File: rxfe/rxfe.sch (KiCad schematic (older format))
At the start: 84 parts, among them J1 SMA, J2 SMA, J3 4610X-AP1-103LF, P1 CONN_8X2, P2 CONN_2, U1 SKY12347, U10 SMP1330-005LF, U11 SMP1330-005LF, U12 SMP1330-005LF, U13 7805, U14 TCM809, U2 74HC04, U3 SCLF-25, U4 HMC595, U5 HMC595, U6 MGA-61563, U7 MGA-61563, U8 HMC595, U9 HMC595

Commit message: cleanups on rxfe
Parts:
- C1, C10, C11, C12, C13, C14, C15, C16, C17, C18, C19, C2, C20, C21, C22, C23, C24, C25, C26, C27, C28, C3, C4, C5, C9, D1, L4, L5, L6, L7, R1, R10, R11, R12, R13, R14, R2, R3, R4, R5, R7, R8, R9: footprint SMD_Packages:SM0805 -> SMD_Packages:SMD-0805
- C31, C32, C33, C34, C35: renamed from C?; footprint SMD_Packages:SM0805 -> SMD_Packages:SMD-0805
- C6, C7, C8, L1, L2, L3: footprint SMD_Packages:SM1210 -> SMD_Packages:SMD-1210
- H1, H2, H3, H4: renamed from H?; footprint (none) -> Mounting_Holes:MountingHole_6-5mm
- J1, J2: footprint sma:sma -> local:SMA_5-1814832-1
- L8: renamed from L?; footprint SMD_Packages:SM0805 -> SMD_Packages:SMD-0805
- P1: footprint Connect:VASCH10x2 -> Connect:VASCH8x2
- R15, R6: renamed from R?; footprint SMD_Packages:SM0805 -> SMD_Packages:SMD-0805
- U10, U11, U12: footprint SMD_Packages:SOT23 -> SMD_Packages:SOT-23
- U13: footprint (none) -> Housings_SOT-89:SOT89-3_Housing
- U14: footprint (none) -> SMD_Packages:SOT-23
- U15: renamed from U?; footprint SMD_Packages:SOT23 -> SMD_Packages:SOT-23
- U4, U5, U8, U9: footprint SMD_Packages:SOT23_6 -> SMD_Packages:SOT-23-6
- gave numbers to parts that had none: 1

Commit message: moved rf amps from control board to rxfe and driver
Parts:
- removed L8: 10 uH, SMD_Packages:SMD-0805, symbol INDUCTOR_SMALL
- removed P2: CONN_2, Connect:PINHEAD1-2, symbol CONN_2
- removed R13: 0, SMD_Packages:SMD-0805, symbol R
- removed R14: DNP, SMD_Packages:SMD-0805, symbol R
- removed R15: 1k, SMD_Packages:SMD-0805, symbol R
- removed U11, U15: SMP1330-005LF, SMD_Packages:SOT-23, symbol SMP1330-005LF
- removed U13: 7805, Housings_SOT-89:SOT89-3_Housing, symbol 7805
- removed U16, U6, U7: MGA-61563, Housings_SOT-23_SOT-143_TSOT-6:SC70-6, symbol MGA-61563
- added C36: 1 uF, SMD_Packages:SMD-0805, symbol C
- added J4: SMA, local:SMA_5-1814832-1, symbol SMA
- added K1: CONN_3, symbol CONN_3
- added U11: LTC1983-5, symbol LTC1983-5
- added U13: LDO_78XX, symbol LDO_78XX
- added U15, U16: GALI-84+, symbol HMC475
- added U6: MAR-8ASM+, symbol MAR-8ASM+
- added U7: SWMA-2-50DR+, symbol SWMA-2-50DR+
- C12, C14: value DNP -> 22 nF
- C15, C17, C21, C4: value 20 nF -> 22 nF
- C16, C18, C20, C22: value 100 pF -> 22 nF
- C19: value 20 nF -> 100 nF
- C31: value 22 nF -> 100 nF
- C32: value 100 pF -> 100 nF
- C33: value 20 nF -> 10 uF
- C34: value 100 pF -> 10 uF
- C35: value 22 nF -> 10 uF; footprint SMD_Packages:SMD-0805 -> SMD_Packages:SMD-1210
- C6: value 22 uF -> 10 uF
- L4, L5: value 0 -> 10 uH
- R10: value 0 -> 309
- R11: value DNP -> 309
- R12: value DNP -> 3.9; footprint SMD_Packages:SMD-0805 -> (none)
- R7: value 1k -> 0
- R9: value 1k -> 309
- U2: footprint SMD_Packages:TSSOP14 -> (none)
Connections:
- net labels added: -5V, T/R, VDD
- wire segments 247 -> 263
- no-connect marks 0 -> 2
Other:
- note added: "-5V switching regulator,\nfor high isolation T/R switch"
- note removed: "jumper to bypass first stage amp"
- moved on the sheet: C1, C10, C11, C13, C15, C17, C2, C23, C24, C25, C26, C29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

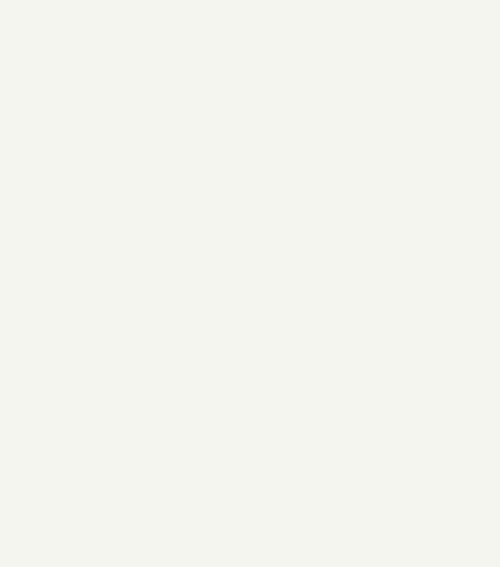
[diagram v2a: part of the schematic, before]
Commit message: DFM changes to boards - added fiducial markers and increase paste clearance
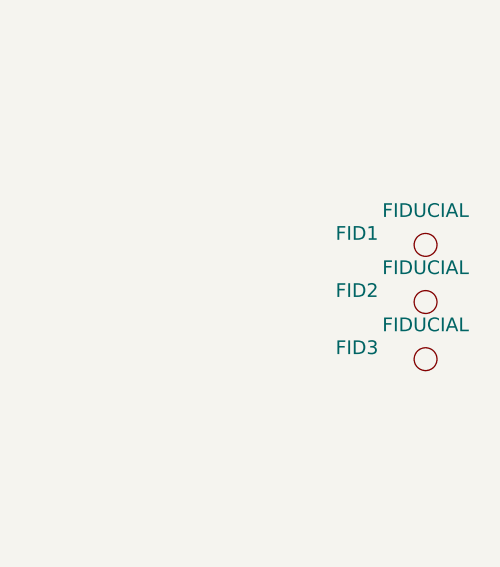
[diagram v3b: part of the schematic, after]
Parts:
- added FID1, FID2, FID3: FIDUCIAL, symbol MOUNTING_HOLE
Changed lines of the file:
@@
 	8450 15000 8450 14900
 Connection ~ 8450 14400
+$Comp
+L MOUNTING_HOLE FID1
+U 1 1 54D26C4B
+P 19650 3950
+F 0 "FID1" H 19350 4000 60  0000 C CNN
+F 1 "FIDUCIAL" H 19650 4100 60  0000 C CNN
+F 2 "" H 19650 3950 60  0000 C CNN
+F 3 "" H 19650 3950 60  0000 C CNN
+	1    19650 3950
+	1    0    0    -1
+$EndComp
+$Comp
+L MOUNTING_HOLE FID2
+U 1 1 54D26C67
+P 19650 4200
+F 0 "FID2" H 19350 4250 60  0000 C CNN
+F 1 "FIDUCIAL" H 19650 4350 60  0000 C CNN
+F 2 "" H 19650 4200 60  0000 C CNN
+F 3 "" H 19650 4200 60  0000 C CNN
+	1    19650 4200
+	1    0    0    -1
+$EndComp
+$Comp
+L MOUNTING_HOLE FID3
+U 1 1 54D26C72
+P 19650 4450
+F 0 "FID3" H 19350 4500 60  0000 C CNN
+F 1 "FIDUCIAL" H 19650 4600 60  0000 C CNN
+F 2 "" H 19650 4450 60  0000 C CNN
+F 3 "" H 19650 4450 60  0000 C CNN
+	1    19650 4450
+	1    0    0    -1
+$EndComp
 $EndSCHEMATC

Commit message: finished layout of DFM'ed driver ampifier board.. except still need to change connectors
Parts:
- C33, C34: footprint SMD_Packages:SMD-0805 -> SMD_Packages:SMD-1210_Pol
- C35: footprint SMD_Packages:SMD-1210 -> SMD_Packages:SMD-1210_Pol
- FID1, FID2, FID3: footprint (none) -> sdtransmitter:FID_1MM
- K1: footprint (none) -> localconn:3-647166-3
- L5, R10, R11, R9: footprint SMD_Packages:SMD-0805 -> SMD_Packages:SMD-1210
- R12: footprint (none) -> SMD_Packages:SMD-0805
- U11: footprint (none) -> SMD_Packages:SOT-23-6
- U13, U15, U16: footprint (none) -> Housings_SOT-89:SOT89-3_Housing
- U2: footprint (none) -> SMD_Packages:TSSOP14
- U6: footprint (none) -> sdtransmitter:WW107
- U7: footprint (none) -> sdtransmitter:DL1020

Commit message: DFM changes..
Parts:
- removed R7: 0, SMD_Packages:SMD-0805, symbol R
- added C37: 22 nF, SMD_Packages:SMD-0805, symbol C
- J1, J2, J4: footprint local:SMA_5-1814832-1 -> local:SMA_0732511350
- K1: footprint localconn:3-647166-3 -> sdtransmitter:0740991003
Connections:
- net at J4.1 (RF), R6.2: now also C37.2
- net at C14.2, R8.2: now also C37.1

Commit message: component footprint changes to simplify bom
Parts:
- removed C33: 10 uF, SMD_Packages:SMD-1210_Pol, symbol C
- removed R12: 3.9, SMD_Packages:SMD-0805, symbol R
- U4, U5, U9: value HMC595 -> MASWSS0179
- U8: value HMC595 -> MASWSS0179'
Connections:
- net -5V: now also C34.2, U11.2 (Vout)
- net GND: no longer U13.2 (GND)

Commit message: DFM changes after last protoype rev
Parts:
- removed C19, C2, C31, C32: 100 nF, SMD_Packages:SMD-0805, symbol C
- added R12, R7: 1k, SMD_Packages:SMD-0805, symbol R
- C1, C29, C5: value 100 nF -> 22 nF
- L4, L5, L6, L7: value 10 uH -> 3.9uH
- R10, R11: value 309 -> 93.1
- R9: value 309 -> 1k; footprint SMD_Packages:SMD-1210 -> SMD_Packages:SMD-0805
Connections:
- net GND: now also U13.2 (GND)
- net VDD: now also R12.1, R7.1
- net at L4.2, R9.2: now also R12.2, R7.2

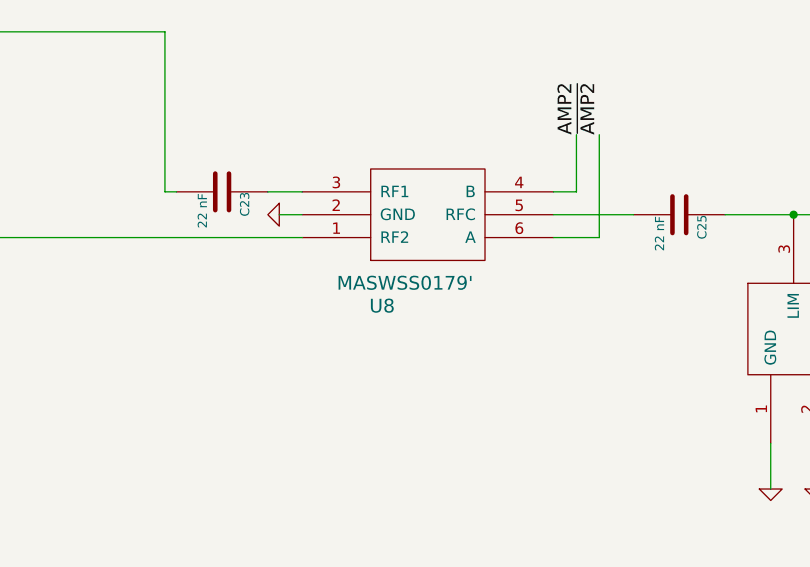
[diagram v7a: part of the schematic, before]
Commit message: updated schematic with distributor part numbers
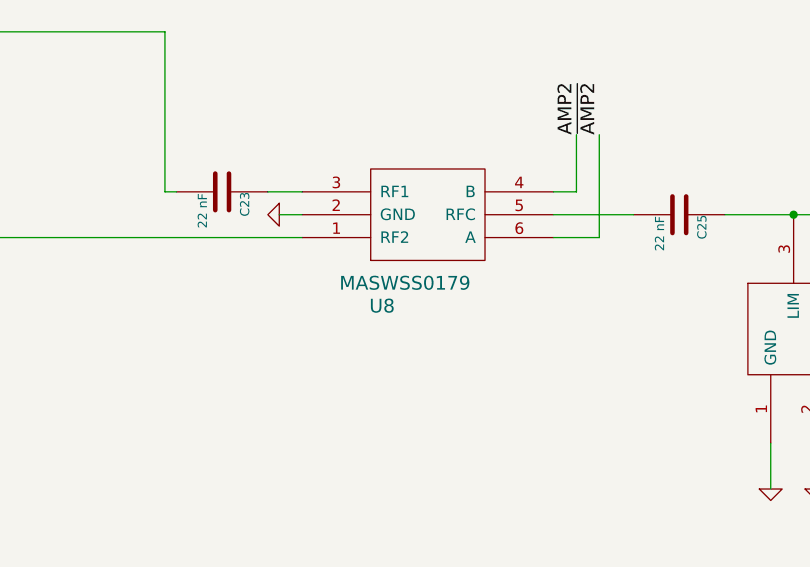
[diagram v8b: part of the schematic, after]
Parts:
- C1, C10, C11, C12, C13, C15, C16, C18, C20, C21, C22, C23, C24, C25, C26, C27, C28, C29, C3, C4, C5, C9: Dist Name (none) -> DigiKey; Dist PN (none) -> 490-1658-1-ND; MFG Name (none) -> MURATA ELECTRONICS (VA); MFG PN (none) -> GRM21BR72A223KA01L
- C14, C37: Dist PN (none) -> 490-1658-1-ND; MFG Name (none) -> MURATA ELECTRONICS (VA); MFG PN (none) -> GRM21BR72A223KA01L
- C17: Dist Name (none) -> DigiKey; MFG Name (none) -> MURATA ELECTRONICS (VA); MFG PN (none) -> GRM21BR72A223KA01L
- C30, C36: Dist Name (none) -> DigiKey; Dist PN (none) -> 445-8782-1-ND; MFG Name (none) -> TDK CORPORATION (VA); MFG PN (none) -> CGA4J3X7S2A105K125AE
- C34, C35: Dist Name (none) -> DigiKey; Dist PN (none) -> 478-3876-1-ND; MFG Name (none) -> AVX CORPORATION (VA); MFG PN (none) -> TAJB106M020RNJ
- C6: footprint SMD_Packages:SMD-1210 -> SMD_Packages:SMD-1210_Pol; Dist Name (none) -> DigiKey; Dist PN (none) -> 478-3876-1-ND; MFG Name (none) -> AVX CORPORATION (VA); MFG PN (none) -> TAJB106M020RNJ
- C7, C8: footprint SMD_Packages:SMD-1210 -> SMD_Packages:SMD-1206_Pol; Dist Name (none) -> DigiKey; Dist PN (none) -> 490-5278-1-ND; MFG Name (none) -> MURATA ELECTRONICS (VA); MFG PN (none) -> GRM31B5C2J681JW01L
- D1: Dist Name (none) -> DigiKey; Dist PN (none) -> 475-1278-1-ND; MFG Name (none) -> OSRAM OPTO SEMICONDUCTORS INC(VA); MFG PN (none) -> LS R976-NR-1
- J1, J2, J4: Dist Name (none) -> DigiKey; Dist PN (none) -> WM9357-ND; MFG Name (none) -> MOLEX INC; MFG PN (none) -> 732511350
- J3: Dist Name (none) -> DigiKey; Dist PN (none) -> 4610X-1-103LF-ND; MFG Name (none) -> BOURNS INC; MFG PN (none) -> 4610X-101-103LF
- K1: Dist Name (none) -> DigiKey; Dist PN (none) -> WM7203-ND; MFG Name (none) -> MOLEX INC; MFG PN (none) -> 740991003
- L1, L3: Dist Name (none) -> DigiKey; Dist PN (none) -> 445-16595-1-ND; MFG Name (none) -> TDK CORPORATION (VA); MFG PN (none) -> NLV32T-3R9J-EFD
- L2: Dist Name (none) -> DigiKey; Dist PN (none) -> PM1210-1R2J-RCCT-ND; MFG Name (none) -> BOURNS INC (VA); MFG PN (none) -> PM1210-1R2J-RC
- L4, L5, L6, L7: Dist Name (none) -> DigiKey
- P1: Dist Name (none) -> DigiKey; Dist PN (none) -> 3M11931-ND; MFG Name (none) -> 3M; MFG PN (none) -> 30316-6002HB
- R1, R12, R2, R3, R4, R5, R7: Dist Name (none) -> DigiKey; Dist PN (none) -> P1.00KCCT-ND; MFG Name (none) -> PANASONIC ELECTRONIC COMPONENTS (VA); MFG PN (none) -> ERJ-6ENF1001V
- R10, R11: Dist Name (none) -> DigiKey; Dist PN (none) -> P93.1FDKR-ND; MFG Name (none) -> PANASONIC ELECTRONIC COMPONENTS (VA); MFG PN (none) -> ERJ-8ENF93R1V
- R9: footprint SMD_Packages:SMD-0805 -> SMD_Packages:SMD-1210; Dist Name (none) -> DigiKey; Dist PN (none) -> P1.00KCCT-ND; MFG Name (none) -> PANASONIC ELECTRONIC COMPONENTS (VA); MFG PN (none) -> ERJ-6ENF1001V
- U1: Dist Name (none) -> DigiKey; Dist PN (none) -> 863-1298-1-ND; MFG Name (none) -> SKYWORKS SOLUTIONS INC (VA); MFG PN (none) -> SKY12347-362LF
- U10, U12: Dist Name (none) -> DigiKey; Dist PN (none) -> 863-1101-1-ND; MFG Name (none) -> SKYWORKS SOLUTIONS INC (VA); MFG PN (none) -> SMP1330-005LF
- U11: Dist Name (none) -> DigiKey; Dist PN (none) -> LTC1983ES6-5#TRMPBFCT-ND; MFG Name (none) -> LINEAR TECHNOLOGY (VA); MFG PN (none) -> LTC1983ES6-5#TRMPBF
- U13: footprint Housings_SOT-89:SOT89-3_Housing -> SMD_Packages:SOT-223; Dist Name (none) -> DigiKey; Dist PN (none) -> 296-12290-1-ND; MFG Name (none) -> TEXAS INSTRUMENTS (VA); MFG PN (none) -> UA78M05CDCYR
- U14: Dist Name (none) -> DigiKey; Dist PN (none) -> TCM809JVNB713CT-ND; MFG Name (none) -> MICROCHIP TECHNOLOGY (VA); MFG PN (none) -> TCM809JVNB713
- U15: Dist Name (none) -> Mini-Circuits
- U16: Dist Name (none) -> Mini-Circuits; Dist PN (none) -> GALI-84+; MFG Name (none) -> Mini-Circuits; MFG PN (none) -> GALI-84+
- U2: Dist Name (none) -> DigiKey; Dist PN (none) -> 296-8208-1-ND; MFG Name (none) -> TEXAS INSTRUMENTS (VA); MFG PN (none) -> SN74HC04PWR
- U3: Dist Name (none) -> Mini-Circuits; Dist PN (none) -> SCLF-25; MFG Name (none) -> Mini-Circuits; MFG PN (none) -> SCLF-25
- U4, U5, U9: Dist Name (none) -> DigiKey; Dist PN (none) -> 1465-1387-1-ND; MFG Name (none) -> M/A-COM TECHNOLOGY SOLUTIONS (VA); MFG PN (none) -> MASWSS0179TR-3000
- U7: Dist Name (none) -> Mini-Circuits; Dist PN (none) -> SWMA-2-50DR+; MFG Name (none) -> Mini-Circuits; MFG PN (none) -> SWMA-2-50DR+
- U8: value MASWSS0179' -> MASWSS0179; Dist Name (none) -> DigiKey; Dist PN (none) -> 1465-1387-1-ND; MFG Name (none) -> M/A-COM TECHNOLOGY SOLUTIONS (VA); MFG PN (none) -> MASWSS0179TR-3000
